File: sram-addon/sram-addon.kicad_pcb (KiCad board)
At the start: 2 copper layers, 39.3 x 29.8 mm, 10 parts, among them J1 Conn_01x02_Male, J10 Conn_01x12_Male, J12 Conn_01x15_Male, J7 Conn_01x09_Male, J8 Conn_01x06_Male, U1 CY62167EV18

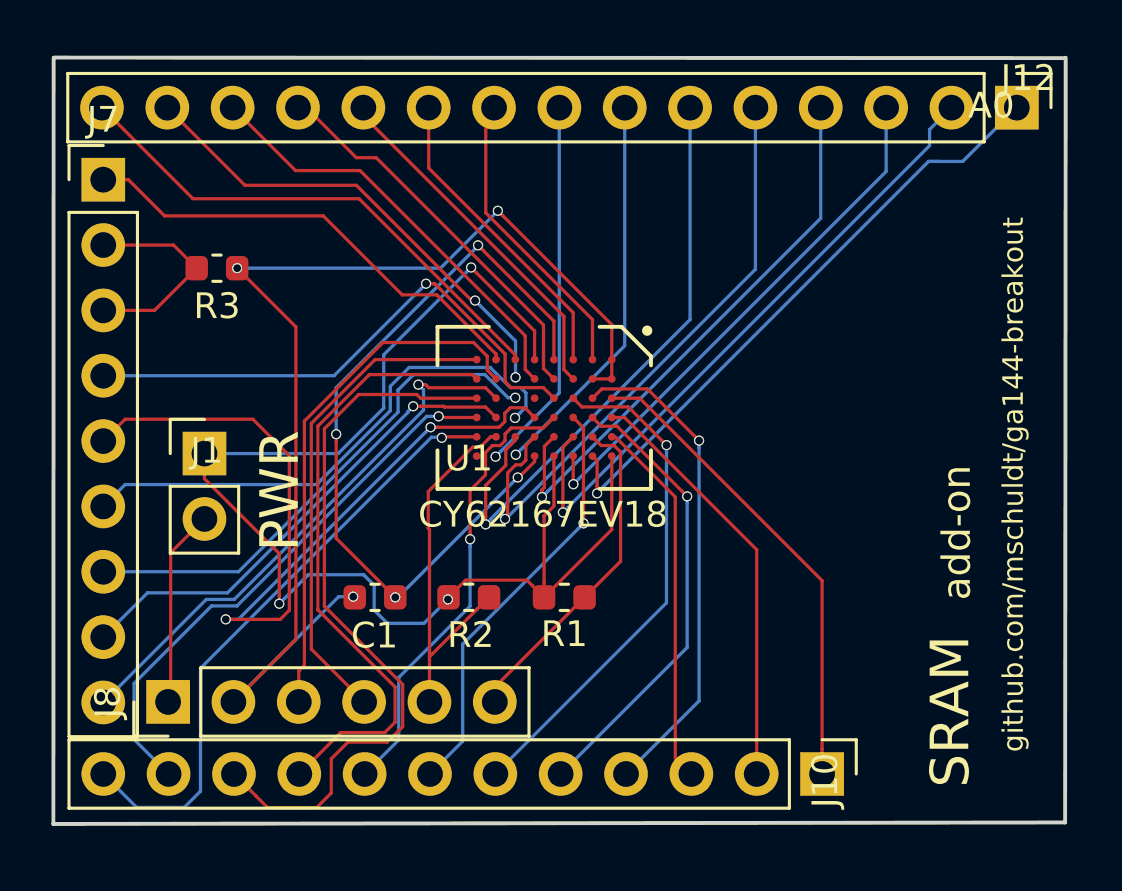
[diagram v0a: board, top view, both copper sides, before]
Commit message: sram-addon: update header
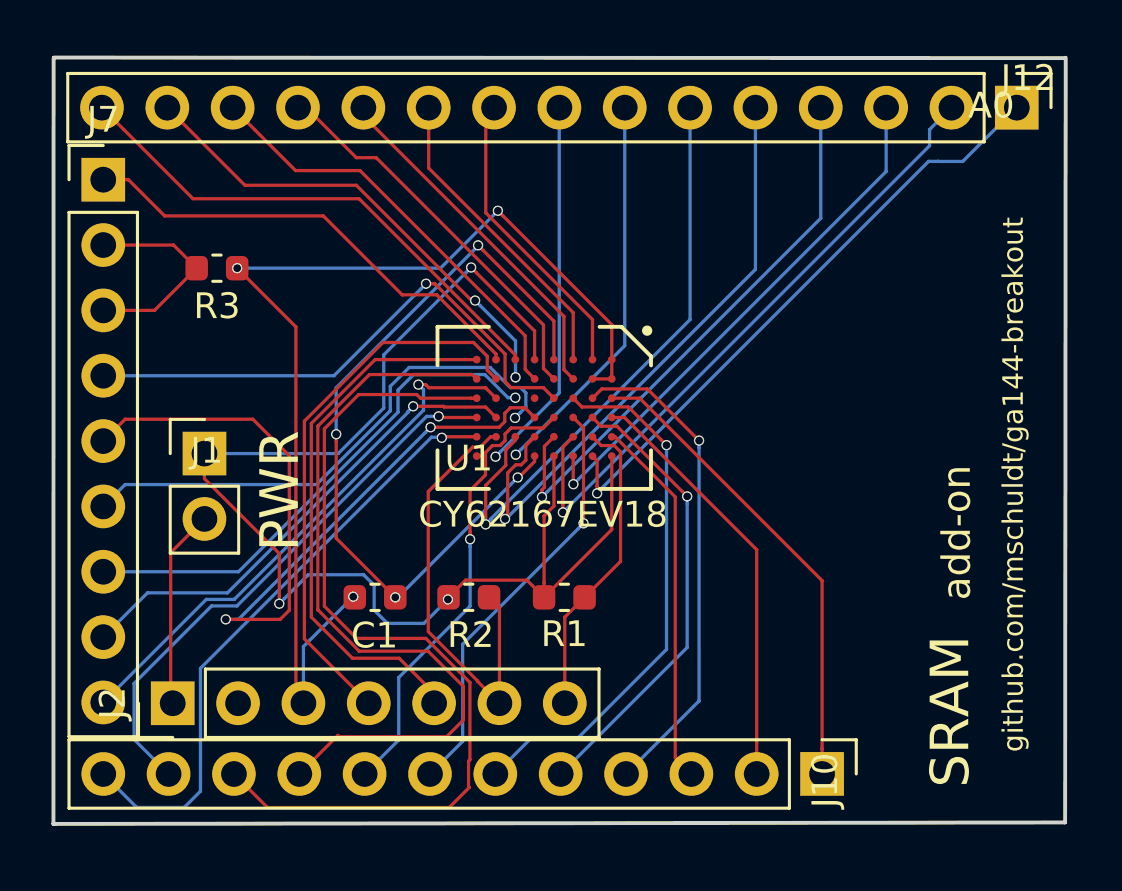
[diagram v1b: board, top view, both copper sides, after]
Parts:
- removed J8: Conn_01x06_Male, Connector_PinHeader_2.54mm:PinHeader_1x06_P2.54mm_Vertical
- added J2: Conn_01x07_Male, Connector_PinHeader_2.54mm:PinHeader_1x07_P2.54mm_Vertical, F.Cu at (112.0, 98.3)
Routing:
- net a9: track 28.6 -> 34.4 mm
- net a8: track 24.4 -> 29.7 mm
- net 008.3: track 15.0 -> 17.8 mm
- net GND: track 45.3 -> 43.1 mm
- net 008.5: track 19.1 -> 21.4 mm
- net 008.1: track 13.1 -> 12.0 mm
- net a5: track 19.9 -> 21.0 mm
- net 008.17: track 20.6 -> 21.6 mm
